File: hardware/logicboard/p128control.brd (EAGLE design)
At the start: 95 x 72 mm, 13 parts

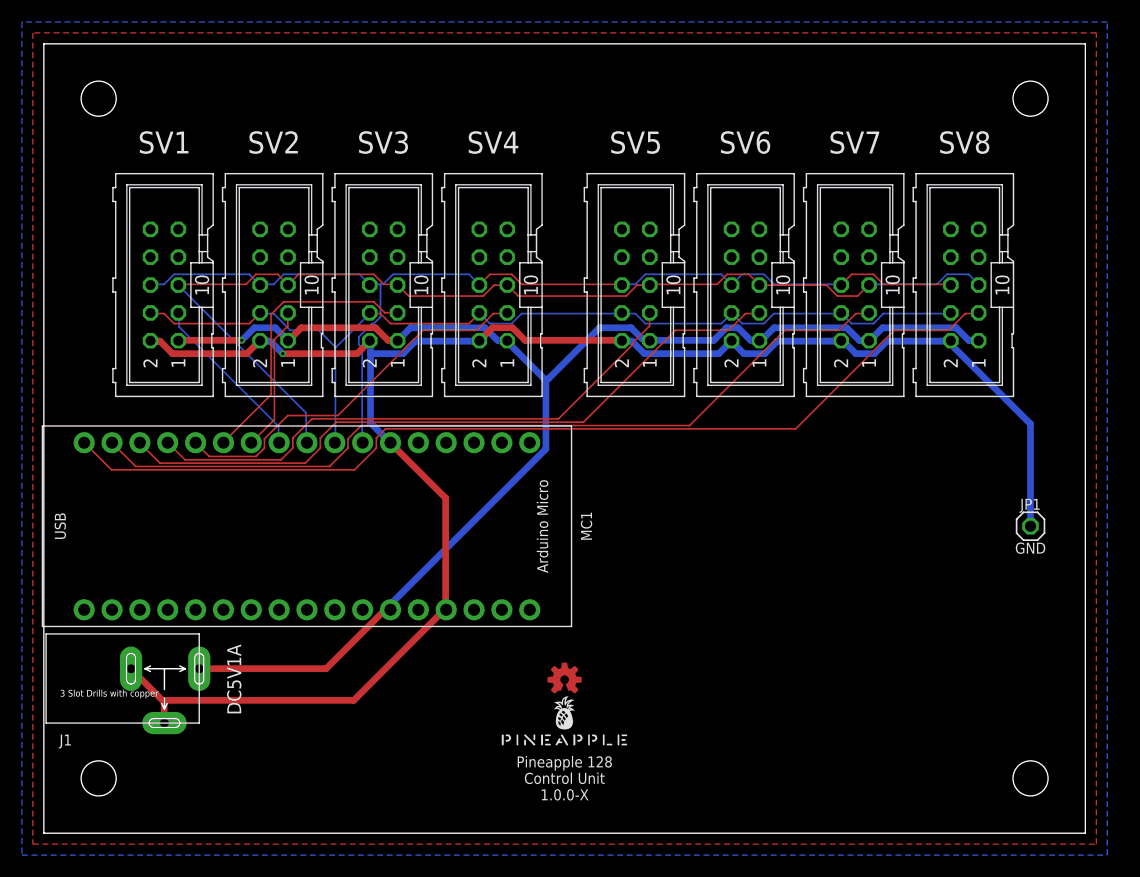
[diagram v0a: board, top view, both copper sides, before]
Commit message: Added MIDI-IN.
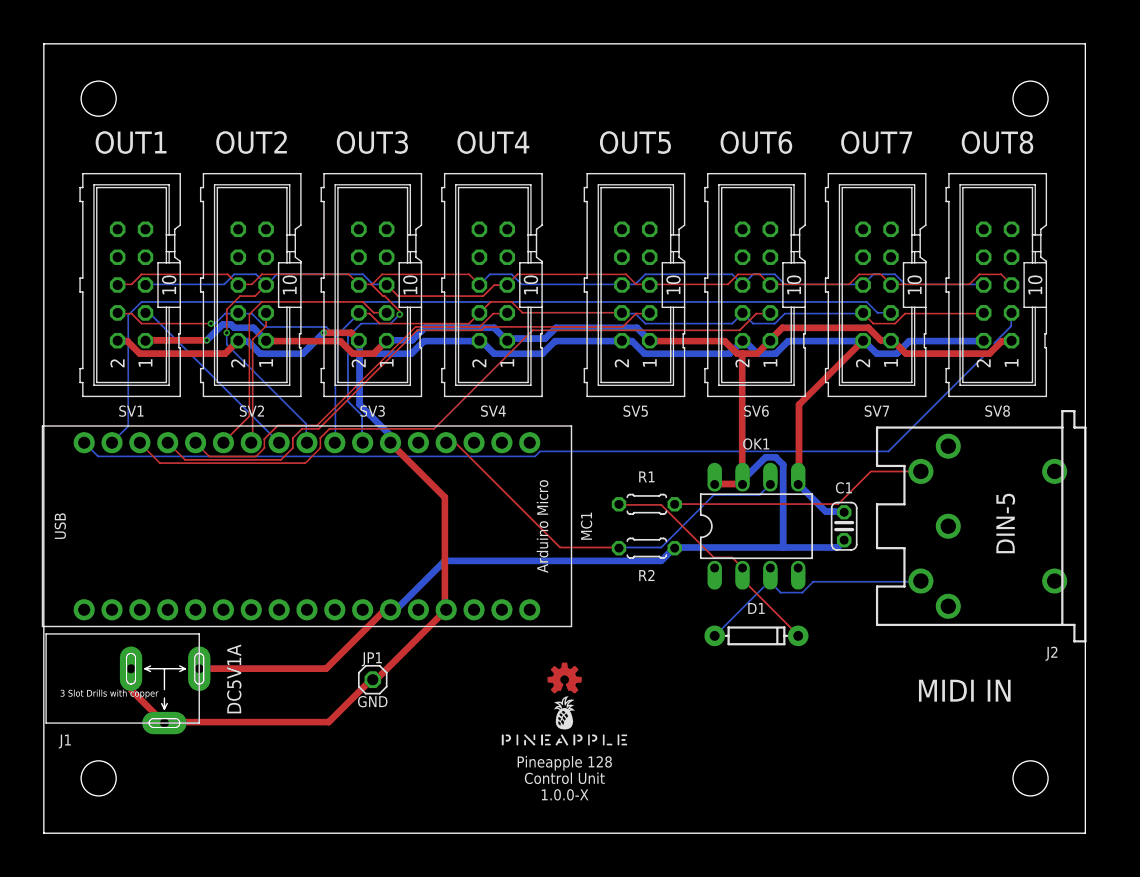
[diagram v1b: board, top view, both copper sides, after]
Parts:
- added C1: (no value), resistor:C025-024X044
- added D1: 200mA/100V/1V, SparkFun-DiscreteSemi:DIODE-1N4148
- added J2: DIN5, SparkFun-Connectors:DIN5-RA-PTH
- added OK1: 6N137, optocoupler:DIL08
- added R1, R2: (no value), resistor:0204/5
- moved JP1 61.6 mm to (30.0, 14.0)
- moved SV1 3.00 mm to (8.00, 50.0)
- moved SV8 3.00 mm to (87.0, 50.0)
- moved SV2 2.00 mm to (19.0, 50.0)
- moved SV7 2.00 mm to (76.0, 50.0)
- moved SV3 1.00 mm to (30.0, 50.0)
- moved SV6 1.00 mm to (65.0, 50.0)
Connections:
- new net MIRETN: D1.A, J2.5, OK1.3
- new net MISEND: J2.4, R1.2
- new net N$1: D1.C, OK1.2, R1.1
- new net RX: OK1.6, R2.1, U$2.P$14
- net GND: now also C1.2, OK1.5
- net VCC: now also C1.1, OK1.7, OK1.8, R2.2
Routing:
- net VCC: track 129.3 -> 177.1 mm
- net RX: track 0.00 -> 36.0 mm
- net MIRETN: track 0.00 -> 24.2 mm
- net MISEND: track 0.00 -> 23.7 mm
- net N$1: track 0.00 -> 22.0 mm
- net CLR: track 94.3 -> 104.5 mm, vias 0 -> 1
- net GND: track 162.1 -> 170.7 mm
- net RCLK: track 98.1 -> 104.6 mm, vias 0 -> 1
- net SOUT7: track 76.2 -> 82.7 mm
- net SCLK: track 89.4 -> 95.6 mm, vias 0 -> 1
- net SOUT8: track 89.1 -> 91.3 mm
- net SOUT1: track 15.7 -> 17.1 mm
- net SOUT6: track 63.5 -> 64.5 mm
- net SOUT2: track 13.2 -> 12.4 mm
- net SOUT5: track 51.5 -> 50.7 mm
- removed copper zone on layer 1, net GND
- removed copper zone on layer 16, net GND
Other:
- board text added: "MIDI IN"
- board text added: "OUT1"
- board text added: "OUT2"
- board text added: "OUT3"
- board text added: "OUT4"
- board text added: "OUT5"
- board text added: "OUT6"
- board text added: "OUT7"
- board text added: "OUT8"

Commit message: Re-designed the controller.
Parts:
- added IC1: 74LS158N, 74xx-us:DIL16
- added RN1: (no value), resistor-dil:DIL16
- added S1, S2: (no value), switch-dil:A1353HEX
- moved U$1 58.0 mm to (47.5, 66.0)
- moved LOGO1 49.0 mm to (47.5, 63.0)
- moved JP1 15.8 mm to (17.0, 5.00)
- moved C1 3.00 mm to (70.0, 28.0)
- moved D1 2.83 mm to (63.0, 20.0)
- moved OK1 2.00 mm to (63.0, 28.0)
- moved R1 1.00 mm to (54.0, 30.0)
- moved R2 1.00 mm to (54.0, 26.0)
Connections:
- new net SW1: IC1.4, U$2.P$31
- new net SW2: IC1.7, U$2.P$30
- new net SW4: IC1.9, U$2.P$29
- new net SW8: IC1.12, U$2.P$28
- new net SWA1: IC1.2, RN1.1, S1.1
- new net SWA2: IC1.5, RN1.3, S1.4
- new net SWA4: IC1.11, RN1.5, S1.8
- new net SWA8: IC1.14, RN1.7, S1.2
- new net SWB1: IC1.3, RN1.2, S2.1
- new net SWB2: IC1.6, RN1.4, S2.4
- new net SWB4: IC1.10, RN1.6, S2.8
- new net SWB8: IC1.13, RN1.8, S2.2
- new net SWSEL: IC1.1, U$2.P$27
- net GND: now also IC1.15, IC1.8, S1.C, S2.C
- net VCC: now also IC1.16, RN1.10, RN1.11, RN1.12, RN1.13, RN1.14, RN1.15, RN1.16, RN1.9
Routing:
- net GND: track 170.7 -> 246.5 mm
- net SWB8: track 0.00 -> 69.0 mm
- net SWB1: track 0.00 -> 61.7 mm
- net SWB2: track 0.00 -> 61.0 mm
- net SWA2: track 0.00 -> 58.8 mm
- net SWA1: track 0.00 -> 56.2 mm
- net SWB4: track 0.00 -> 46.3 mm
- net SWA8: track 0.00 -> 46.1 mm
- net SWA4: track 0.00 -> 36.2 mm
- net SW2: track 0.00 -> 28.4 mm
- net SW4: track 0.00 -> 28.4 mm
- net SW1: track 0.00 -> 22.9 mm
- net CLR: track 104.5 -> 123.7 mm, vias 1 -> 0
- net VCC: track 177.1 -> 192.6 mm
- net SW8: track 0.00 -> 14.7 mm
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- added copper zone on layer 1, net GND
- added copper zone on layer 16, net GND
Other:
- board text added: "A"
- board text added: "B"

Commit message: SW.
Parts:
- added C2: (no value), resistor:C025-024X044
- R1: value (none) -> 220
- R2, RN1: value (none) -> 10k
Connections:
- net GND: now also C2.2
- net VCC: now also C2.1
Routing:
- net VCC: track 192.6 -> 211.1 mm
- net SWB8: track 69.0 -> 55.5 mm
- net GND: track 246.5 -> 254.0 mm
- net SWA2: track 58.8 -> 53.3 mm
- net SWB1: track 61.7 -> 65.4 mm
- net SWA8: track 46.1 -> 48.2 mm
- net SWB2: track 61.0 -> 59.9 mm
- net SWA4: track 36.2 -> 35.5 mm
- net SWA1: track 56.2 -> 56.0 mm, vias 0 -> 1

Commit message: Release candidate.
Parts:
- added JP2: (no value), pinhead:1X06
- moved R1 5.39 mm to (59.0, 32.0), turned to 90 degrees
- moved R2 5.39 mm to (59.0, 24.0), turned to 90 degrees
- moved C1 4.00 mm to (74.0, 28.0)
- moved D1 4.00 mm to (67.0, 20.0)
- moved OK1 4.00 mm to (67.0, 28.0)
- moved J1 1.00 mm to (11.0, 14.0)
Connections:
- new net TX: JP2.5, U$2.P$15
- net GND: now also JP2.1, JP2.2
- net RX: now also JP2.4
- net VCC: now also JP2.3
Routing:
- net GND: track 254.0 -> 289.8 mm, vias 1 -> 2
- net SWB1: track 65.4 -> 83.6 mm, vias 0 -> 1
- net TX: track 0.00 -> 16.4 mm
- net SWA1: track 56.0 -> 68.1 mm
- net RX: track 34.0 -> 44.0 mm
- net SWB8: track 55.5 -> 63.3 mm
- net SWA2: track 53.3 -> 59.6 mm
- net MISEND: track 26.4 -> 21.6 mm
- net SWB2: track 59.9 -> 55.4 mm, vias 0 -> 1
- net MIRETN: track 23.9 -> 19.9 mm
- net N$1: track 19.5 -> 15.8 mm
- net VCC: track 211.1 -> 214.8 mm
- net SOUT5: track 50.7 -> 53.9 mm
- net SOUT6: track 66.0 -> 64.3 mm
- net SWA4: track 35.5 -> 36.9 mm
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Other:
- board text added: "10k"
- board text added: "220"
- board text added: "BK"
- board text added: "BN"
- board text added: "GR"
- board text added: "OR"
- board text added: "RD"
- board text added: "YL"
